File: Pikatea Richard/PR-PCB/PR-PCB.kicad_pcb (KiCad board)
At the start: 2 copper layers, 62 x 136.7 mm, 7 parts, among them SW1 Rotary_Encoder_Switch, SW2 Rotary_Encoder_Switch

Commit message: updated footprints added gerbers
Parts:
- added U1: ProMicro, promicro:ProMicro, F.Cu at (138.2, 3.70)
- moved SW1 2.00 mm to (155.0, 100.0)
- moved SW2 2.00 mm to (123.0, 100.0)
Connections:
- MX2 pad 1: Net-(MX2-Pad1) -> Net-(MX1-Pad1)
- MX3 pad 1: Net-(MX3-Pad1) -> Net-(MX1-Pad1)
- MX4 pad 1: Net-(MX4-Pad1) -> Net-(MX1-Pad1)
- MX5 pad 1: Net-(MX5-Pad1) -> Net-(MX1-Pad1)
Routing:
- net Net-(MX1-Pad1): track 0.00 -> 123.9 mm
- net Net-(MX1-Pad2): track 0.00 -> 64.6 mm
- net Net-(MX2-Pad2): track 0.00 -> 53.7 mm, vias 0 -> 1
- net Net-(MX3-Pad2): track 0.00 -> 30.8 mm
- net Net-(MX4-Pad2): track 0.00 -> 18.1 mm
- net Net-(MX5-Pad2): track 0.00 -> 5.02 mm
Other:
- board size 62 x 136.7 mm -> 56.1 x 120 mm

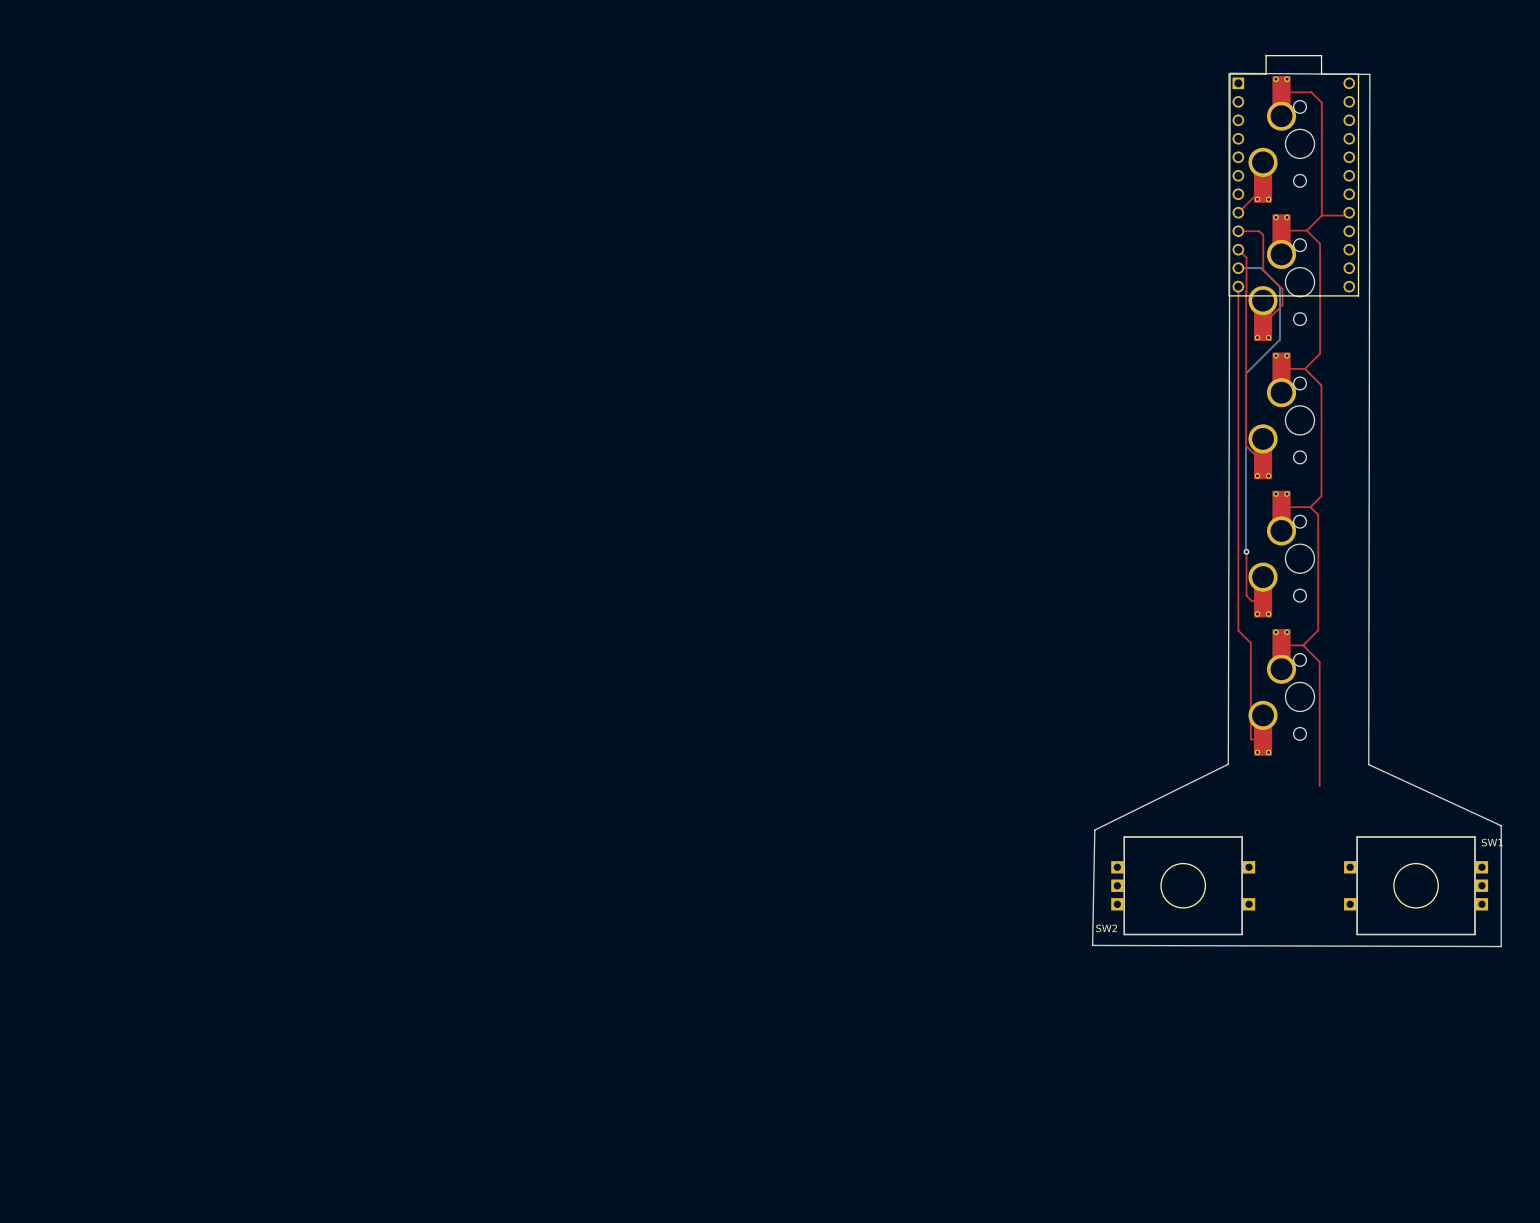
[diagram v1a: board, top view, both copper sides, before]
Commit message: update gb4 to kicad 6, add gb4 fkvarient
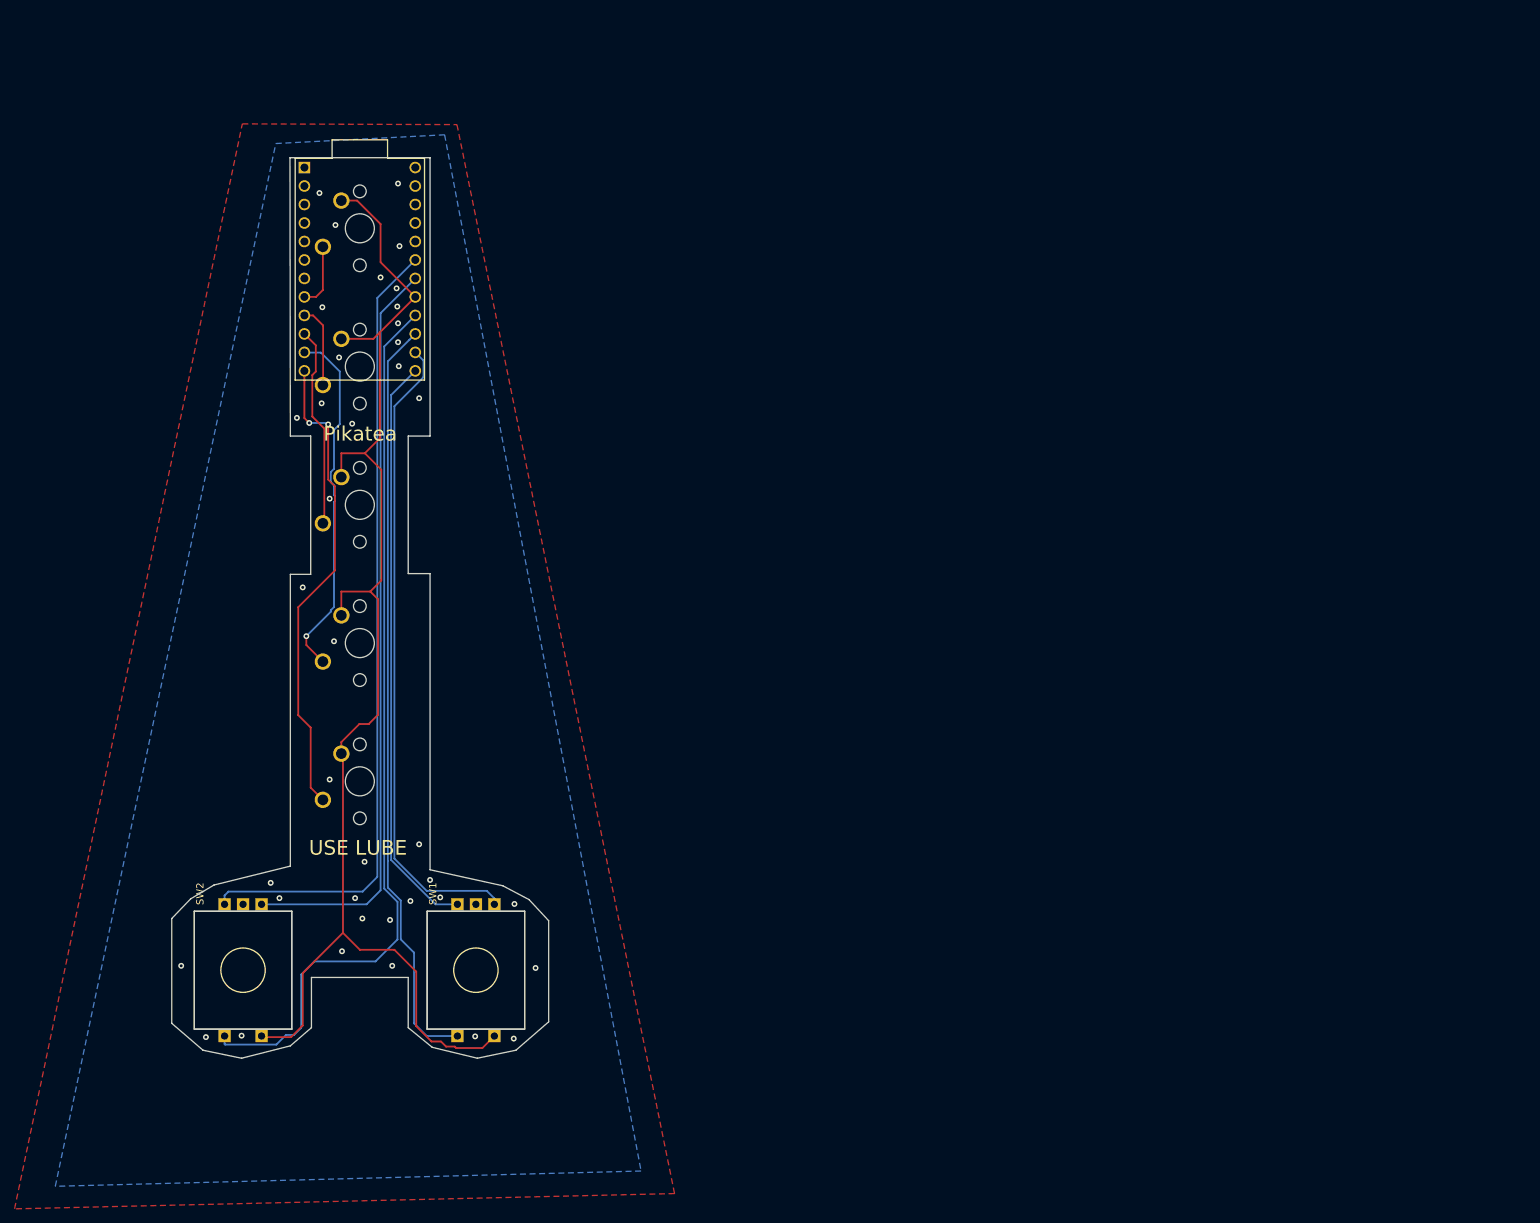
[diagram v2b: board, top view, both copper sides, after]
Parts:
- MX1, MX2, MX3, MX4, MX5: footprint MX_Only:MXOnly-1U-Hotswap-Antishear -> MX_Only:MXOnly-1U-NoLED
- moved MX1 129.7 mm to (9.85, 85.7)
- moved MX2 129.7 mm to (9.85, 66.7)
- moved MX3 129.7 mm to (9.85, 47.6)
- moved MX4 129.7 mm to (9.85, 28.6)
- moved MX5 129.7 mm to (9.85, 9.65)
- moved SW1 129.7 mm to (25.8, 111.6), turned to 270 degrees
- moved SW2 129.7 mm to (-6.20, 111.6), turned to 270 degrees
- moved U1 128.9 mm to (9.85, 15.3)
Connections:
- SW1 pad C: Net-(SW1-PadC) -> GND
- SW1 pad S1: Net-(SW1-PadS1) -> Net-(MX1-Pad1)
- SW2 pad C: Net-(SW2-PadC) -> GND
- SW2 pad S1: Net-(SW2-PadS1) -> Net-(MX1-Pad1)
- U1 pad 13: Net-(U1-Pad13) -> Net-(SW1-PadA)
- U1 pad 14: Net-(U1-Pad14) -> Net-(SW1-PadB)
- U1 pad 15: Net-(U1-Pad15) -> Net-(SW1-PadS2)
- U1 pad 16: Net-(U1-Pad16) -> Net-(SW2-PadS2)
- U1 pad 18: Net-(U1-Pad18) -> Net-(SW2-PadB)
- U1 pad 19: Net-(U1-Pad19) -> Net-(SW2-PadA)
- U1 pad 23: Net-(U1-Pad23) -> GND
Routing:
- net Net-(SW2-PadS2): track 0.00 -> 123.4 mm
- net Net-(SW2-PadA): track 0.00 -> 110.2 mm
- net Net-(SW1-PadS2): track 0.00 -> 104.5 mm
- net Net-(SW2-PadB): track 0.00 -> 103.2 mm
- net Net-(SW1-PadB): track 0.00 -> 88.5 mm
- net Net-(SW1-PadA): track 0.00 -> 80.2 mm
- net Net-(MX1-Pad1): track 123.9 -> 187.2 mm
- net Net-(MX4-Pad2): track 18.1 -> 11.3 mm
- net Net-(MX2-Pad2): track 53.7 -> 49.1 mm
- net Net-(MX5-Pad2): track 5.02 -> 8.87 mm
- net Net-(MX3-Pad2): track 30.8 -> 27.6 mm
- net Net-(MX1-Pad2): track 64.6 -> 65.6 mm, vias 0 -> 2
- net GND: vias 0 -> 39
- added copper zone on B.Cu, net GND
- added copper zone on F.Cu, net GND
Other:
- board size 56.1 x 120 mm -> 51.8 x 123.8 mm
- board text added: "Pikatea"
- board text added: "USE LUBE"
